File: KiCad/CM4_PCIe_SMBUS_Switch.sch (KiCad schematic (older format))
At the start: 2 parts, among them U17 TCA9548ARGER

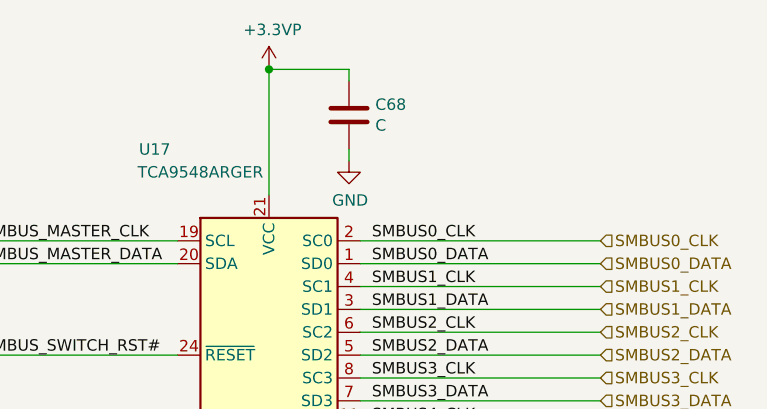
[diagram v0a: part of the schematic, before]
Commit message: PCIe Wiring, resistor value adjustments, and a bunch of small ERC fixes.
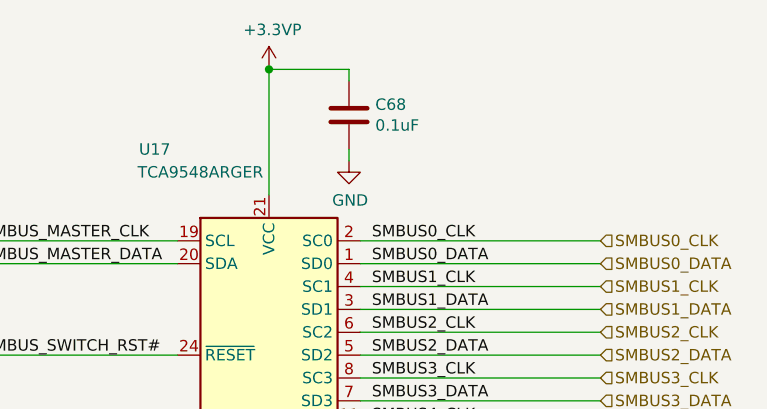
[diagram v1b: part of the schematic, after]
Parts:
- C68: value C -> 0.1uF
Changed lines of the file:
@@
 $Descr A4 11693 8268
 encoding utf-8
-Sheet 14 16
+Sheet 16 16
 Title ""
 Date ""
@@
 P 6100 2350
 F 0 "C68" H 6215 2396 50  0000 L CNN
-F 1 "C" H 6215 2305 50  0000 L CNN
+F 1 "0.1uF" H 6215 2305 50  0000 L CNN
 F 2 "" H 6138 2200 50  0001 C CNN
 F 3 "~" H 6100 2350 50  0001 C CNN

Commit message: Started picking passive components, overhauled library
Cleaned up a bunch of schematic library references.
Added datasheets, descriptions for a lot of existing parts.
Picked most capacitor parts, still a couple left.
Cleaned up a fair few footprint references.
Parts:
- C68: value 0.1uF -> 100nF; footprint (none) -> CM4_MATX:C_0402_1005Metric_Pad0.74x0.62mm_HandSolder; Description (none) -> 10V 0.1uF X5R 0402 20% Tol; Mfr. (none) -> AVX; Mfr. No (none) -> 0402ZD104MAT4A; Mouser Part Number (none) -> 581-0402ZD104MAT4A; Mouser Price/Stock (none) -> https://www.mouser.co.uk/ProductDetail/AVX/0402ZD104MAT4A/?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
- U17: footprint Package_DFN_QFN:Texas_RGE0024C_EP2.1x2.1mm -> CM4_MATX:Texas_RGE0024C_EP2.1x2.1mm; symbol Interface_Expansion:TCA9548ARGER -> CM4_MATX:TCA9548ARGER; Description (none) -> 8-CH I2C Switch w/ Reset; Mfr. (none) -> Texas Instruments; Mfr. No (none) -> TCA9548ARGER; Mouser Part Number (none) -> 595-TCA9548ARGER; Mouser Price/Stock (none) -> https://www.mouser.co.uk/ProductDetail/Texas-Instruments/TC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
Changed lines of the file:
@@
 $Descr A4 11693 8268
 encoding utf-8
-Sheet 16 16
+Sheet 12 16
 Title ""
 Date "2021-02-08"
@@
 $EndDescr
 $Comp
-L Interface_Expansion:TCA9548ARGER U17
+L CM4_MATX:TCA9548ARGER U17
 U 1 1 6002AC4E
 P 5750 3600
 F 0 "U17" H 5250 4700 50  0000 C CNN
 F 1 "TCA9548ARGER" H 5450 4600 50  0000 C CNN
-F 2 "Package_DFN_QFN:Texas_RGE0024C_EP2.1x2.1mm" H 5750 2600 50  0001 C CNN
+F 2 "CM4_MATX:Texas_RGE0024C_EP2.1x2.1mm" H 5750 2600 50  0001 C CNN
 F 3 "http://www.ti.com/lit/ds/symlink/tca9548a.pdf" H 5800 3850 50  0001 C CNN
+F 4 "Texas Instruments" H 5750 3600 50  0001 C CNN "Mfr."
+F 5 "TCA9548ARGER" H 5750 3600 50  0001 C CNN "Mfr. No"
+F 6 "595-TCA9548ARGER" H 5750 3600 50  0001 C CNN "Mouser Part Number"
+F 7 "https://www.mouser.co.uk/ProductDetail/Texas-Instruments/TCA9548ARGER/?qs=2I4pGxj2dxUewY0zSIpfWQ%3D%3D" H 5750 3600 50  0001 C CNN "Mouser Price/Stock"
+F 8 "8-CH I2C Switch w/ Reset" H 5750 3600 50  0001 C CNN "Description"
 	1    5750 3600
 	1    0    0    -1
@@
 SMBUS7_DATA
 $Comp
-L power:+3.3VP #PWR0212
+L CM4_MATX:+3.3VP #PWR0212
 U 1 1 601F4D03
 P 5750 2150
@@
 P 6100 2350
 F 0 "C68" H 6215 2396 50  0000 L CNN
-F 1 "0.1uF" H 6215 2305 50  0000 L CNN
-F 2 "" H 6138 2200 50  0001 C CNN
-F 3 "~" H 6100 2350 50  0001 C CNN
+F 1 "100nF" H 6215 2305 50  0000 L CNN
+F 2 "CM4_MATX:C_0402_1005Metric_Pad0.74x0.62mm_HandSolder" H 6138 2200 50  0001 C CNN
+F 3 "https://www.mouser.co.uk/datasheet/2/40/cx5r-776519.pdf" H 6100 2350 50  0001 C CNN
+F 4 "581-0402ZD104MAT4A" H 6100 2350 50  0001 C CNN "Mouser Part Number"
+F 5 "https://www.mouser.co.uk/ProductDetail/AVX/0402ZD104MAT4A/?qs=sGAEpiMZZMvsSlwiRhF8qud6rLLpfNdE%2FYSoyEGdkn4%3D" H 6100 2350 50  0001 C CNN "Mouser Price/Stock"
+F 6 "AVX" H 6100 2350 50  0001 C CNN "Mfr."
+F 7 "0402ZD104MAT4A" H 6100 2350 50  0001 C CNN "Mfr. No"
+F 8 "10V 0.1uF X5R 0402 20% Tol" H 6100 2350 50  0001 C CNN "Description"
 	1    6100 2350
 	1    0    0    -1
